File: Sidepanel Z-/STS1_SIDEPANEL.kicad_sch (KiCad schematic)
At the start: 5 parts, among them J1 Conn_02x04_Odd_Even, J2 Conn_02x02_Odd_Even

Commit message: Review Ready for V2.0
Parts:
- J1: value Conn_02x04_Odd_Even -> (none); footprint SamacSys:M808280842 -> (none)
- J2: value Conn_02x02_Odd_Even -> (none); footprint USER_Passiv:M80-8280442 -> (none)
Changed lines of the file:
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@@
     (in_bom yes) (on_board yes) (fields_autoplaced)
     (property "Reference" "J1" (id 0) (at 40.64 60.96 0))
-    (property "Value" "Conn_02x04_Odd_Even" (id 1) (at 40.64 63.5 0))
-    (property "Footprint" "SamacSys:M808280842" (id 2) (at 39.37 69.85 0)
+    (property "Value" "" (id 1) (at 40.64 63.5 0))
+    (property "Footprint" "" (id 2) (at 39.37 69.85 0)
       (effects (font (size 1.27 1.27)) hide)
     )
@@
     (in_bom yes) (on_board yes) (fields_autoplaced)
     (property "Reference" "J2" (id 0) (at 86.36 66.04 0))
-    (property "Value" "Conn_02x02_Odd_Even" (id 1) (at 86.36 68.58 0))
-    (property "Footprint" "USER_Passiv:M80-8280442" (id 2) (at 85.09 72.39 0)
+    (property "Value" "" (id 1) (at 86.36 68.58 0))
+    (property "Footprint" "" (id 2) (at 85.09 72.39 0)
       (effects (font (size 1.27 1.27)) hide)
     )
@@
     (path "/" (page "1"))
     (path "/9d03bb93-a9aa-424f-bd25-022f173efd1d" (page "3"))
+    (path "/4f87559b-6bba-4ff6-97a7-dad9a308db2d" (page "4"))
     (path "/13fd01c2-9c13-4b4c-bd8b-0bea989ca11e" (page "4"))
-    (path "/4f87559b-6bba-4ff6-97a7-dad9a308db2d" (page "4"))
   )
   (symbol_instances
@@
     )
     (path "/4f87559b-6bba-4ff6-97a7-dad9a308db2d/934b6342-5d8d-49da-bf4f-f7fa77f16f34"
-      (reference "CUR1") (unit 1) (value "TMCS1101A3BQDT") (footprint "SOIC127P600X175-8N")
+      (reference "CUR1") (unit 1) (value "TMCS1101A3BQDT") (footprint "Package_SO:SOIC-8_3.9x4.9mm_P1.27mm")
     )
     (path "/4f87559b-6bba-4ff6-97a7-dad9a308db2d/bf187b1f-09ac-46cb-aea3-5e2484509796"
-      (reference "CUR2") (unit 1) (value "TMCS1101A3BQDT") (footprint "SOIC127P600X175-8N")
+      (reference "CUR2") (unit 1) (value "TMCS1101A3BQDT") (footprint "Package_SO:SOIC-8_3.9x4.9mm_P1.27mm")
     )
     (path "/4f87559b-6bba-4ff6-97a7-dad9a308db2d/a554cf31-0806-4740-ba0b-f0d59599f4ca"
@@
     )
     (path "/4f87559b-6bba-4ff6-97a7-dad9a308db2d/c6a198d2-e0e4-4d6d-8a2a-bdeb249501be"
-      (reference "DOUT1") (unit 1) (value "SMM4F5.0") (footprint "SamacSys:STMITE")
+      (reference "DOUT1") (unit 1) (value "SMM4F5.0") (footprint "Diode_SMD:D_0603_1608Metric")
     )
     (path "/4f87559b-6bba-4ff6-97a7-dad9a308db2d/65c76957-ccfc-4d5b-b7d9-2ee7c354f524"
-      (reference "DOUT2") (unit 1) (value "SMM4F5.0") (footprint "SamacSys:STMITE")
+      (reference "DOUT2") (unit 1) (value "SMM4F5.0") (footprint "LED_SMD:LED_0603_1608Metric")
     )
     (path "/9d03bb93-a9aa-424f-bd25-022f173efd1d/d9839939-8918-48f3-b4b2-d753b1d9a645"
-      (reference "IC1") (unit 1) (value "TMP112AQDRLRQ1") (footprint "SamacSys:SOTFL50P160X60-6N")
+      (reference "IC1") (unit 1) (value "TMP112AQDRLRQ1") (footprint "Package_TO_SOT_SMD:SOT-563")
     )
     (path "/7d4ab197-adca-450c-9fc5-7a95ff72b885"
-      (reference "J1") (unit 1) (value "Conn_02x04_Odd_Even") (footprint "SamacSys:M808280842")
+      (reference "J1") (unit 1) (value "Conn_02x04_Odd_Even") (footprint "STS_Connector:M808280842")
     )
     (path "/9272ccd5-e950-4f99-baec-47da7f19129b"
-      (reference "J2") (unit 1) (value "Conn_02x02_Odd_Even") (footprint "USER_Passiv:M80-8280442")
+      (reference "J2") (unit 1) (value "Conn_02x02_Odd_Even") (footprint "STS_Connector:M808280442")
     )
     (path "/4f87559b-6bba-4ff6-97a7-dad9a308db2d/bfe4e68f-4cef-4b31-adff-8df094bc3870"
-      (reference "L_IN1") (unit 1) (value "10u") (footprint "SamacSys:INDPM5650X530N")
+      (reference "L_IN1") (unit 1) (value "10u") (footprint "Inductor_SMD:L_0805_2012Metric")
     )
     (path "/4f87559b-6bba-4ff6-97a7-dad9a308db2d/06a966cd-4913-436b-a217-7ac14ca6801e"
-      (reference "L_IN2") (unit 1) (value "10u") (footprint "SamacSys:INDPM5650X530N")
+      (reference "L_IN2") (unit 1) (value "10u") (footprint "Inductor_SMD:L_0805_2012Metric")
     )
     (path "/4f87559b-6bba-4ff6-97a7-dad9a308db2d/679b2e27-da22-4f13-a86e-25be83598a10"
-      (reference "MPPT1") (unit 1) (value "SPV1040TTR") (footprint "SamacSys:SOP65P640X120-8N")
+      (reference "MPPT1") (unit 1) (value "SPV1040TTR") (footprint "Package_SO:TSSOP-8_4.4x3mm_P0.65mm")
     )
     (path "/4f87559b-6bba-4ff6-97a7-dad9a308db2d/f7af2bb9-8bee-4408-8a96-0d5862b66a63"
-      (reference "MPPT2") (unit 1) (value "SPV1040TTR") (footprint "SamacSys:SOP65P640X120-8N")
+      (reference "MPPT2") (unit 1) (value "SPV1040TTR") (footprint "Package_SO:TSSOP-8_4.4x3mm_P0.65mm")
     )
     (path "/6503b427-07c6-4391-8fa6-4757fb4daa6c"
@@
     )
     (path "/4f87559b-6bba-4ff6-97a7-dad9a308db2d/e7b54c2f-482e-4a97-841f-62a80e0193a8"
-      (reference "SC1") (unit 1) (value "Solar_Cell") (footprint "USER_Activ:3G30A_40x80")
+      (reference "SC1") (unit 1) (value "Solar_Cell") (footprint "STS_Connector:3G30A_40x80")
     )
     (path "/4f87559b-6bba-4ff6-97a7-dad9a308db2d/3ad17c33-30d5-4097-824f-a9c26e6ca325"
-      (reference "SC2") (unit 1) (value "Solar_Cell") (footprint "USER_Activ:3G30A_40x80")
+      (reference "SC2") (unit 1) (value "Solar_Cell") (footprint "STS_Connector:3G30A_40x80")
     )
     (path "/e6cad5c9-4a9d-4066-8345-4481317e7bc0"
@@
     )
     (path "/9d03bb93-a9aa-424f-bd25-022f173efd1d/a83d6342-0e16-4131-8bb9-e65e4d72dab0"
-      (reference "U1") (unit 1) (value "GUVA-C32SM") (footprint "USER_Optic:OLGA 2mm x 2,3mm")
-    )
-  )
+      (reference "U1") (unit 1) (value "GUVA-C32SM") (footprint "Package_SO:SO-4_4.4x3.6mm_P2.54mm")
+    )
+  )

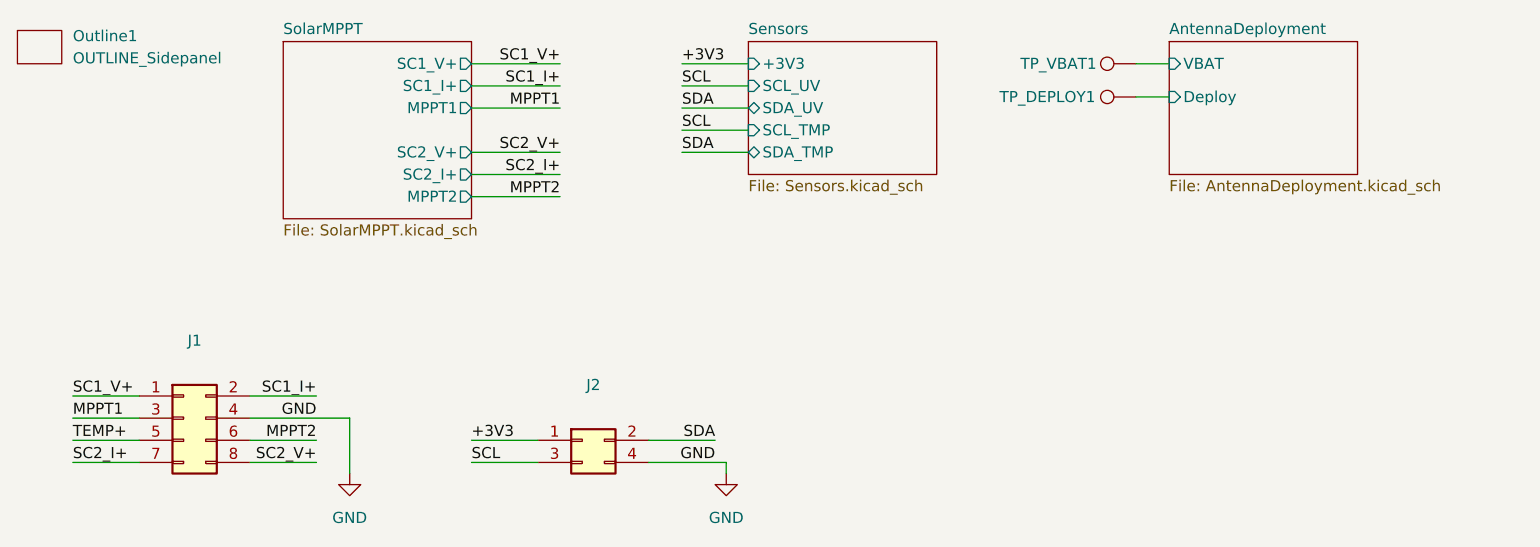
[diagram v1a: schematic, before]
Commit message: Paar Fehler behoben, Z+ no MOSFET
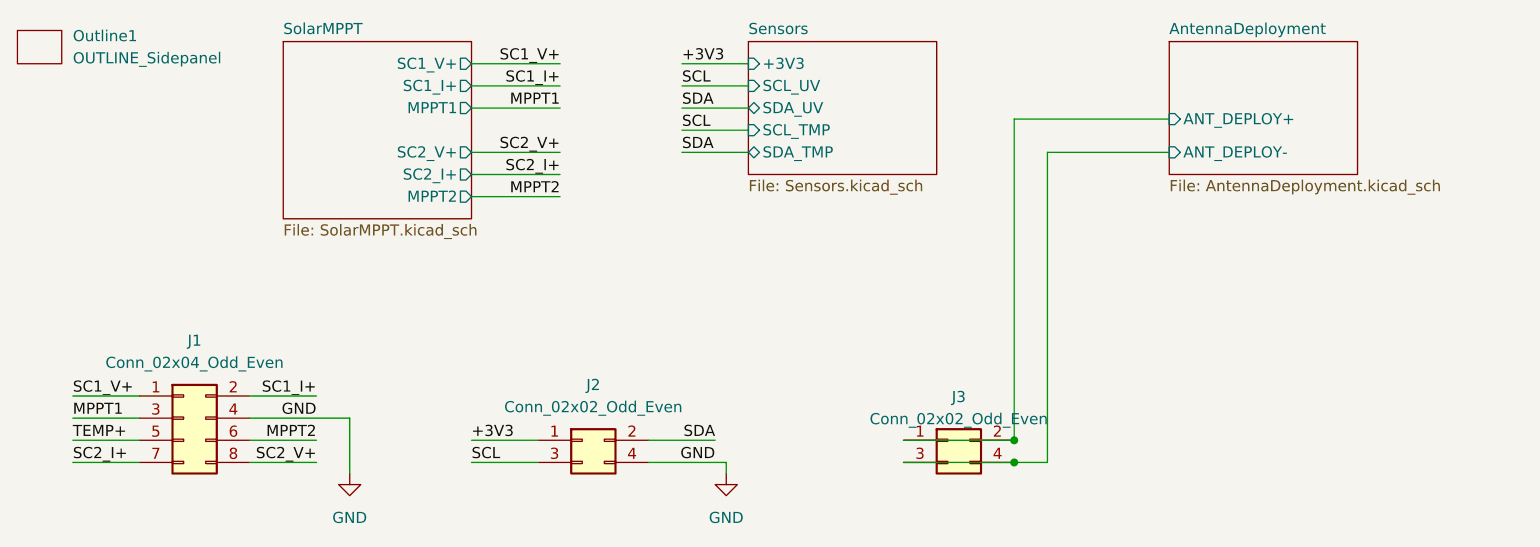
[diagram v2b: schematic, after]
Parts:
- removed TP_DEPLOY1, TP_VBAT1: TestPoint, TestPoint:TestPoint_Loop_D1.80mm_Drill1.0mm_Beaded, symbol Connector:TestPoint
- added J3: Conn_02x02_Odd_Even, STS_Connector:M808280442, symbol Connector_Generic:Conn_02x02_Odd_Even
- J1: value (none) -> Conn_02x04_Odd_Even; footprint (none) -> STS_Connector:M808280842
- J2: value (none) -> Conn_02x02_Odd_Even; footprint (none) -> STS_Connector:M808280442
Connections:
- new net AntennaDeployment/ANT_DEPLOY+: J3.1 (Pin_1), J3.2 (Pin_2)
- new net AntennaDeployment/ANT_DEPLOY-: J3.3 (Pin_3), J3.4 (Pin_4)
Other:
- sheet AntennaDeployment ports: added ANT_DEPLOY+, ANT_DEPLOY-; removed Deploy, VBAT
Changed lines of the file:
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@@
 (kicad_sch (version 20211123) (generator eeschema)
   (paper "A4")
+  (junction (at 134.62 74.93) (diameter 0) (color 0 0 0 0)
+  )
+  (junction (at 134.62 72.39) (diameter 0) (color 0 0 0 0)
+  )
+  (wire (pts (xy 121.92 74.93) (xy 134.62 74.93))
+    (stroke (width 0) (type default) (color 0 0 0 0))
+  )
   (wire (pts (xy 26.67 67.31) (xy 34.29 67.31))
     (stroke (width 0) (type default) (color 0 0 0 0))
   )
+  (wire (pts (xy 138.43 39.37) (xy 152.4 39.37))
+    (stroke (width 0) (type default) (color 0 0 0 0))
+  )
   (wire (pts (xy 54.61 74.93) (xy 46.99 74.93))
     (stroke (width 0) (type default) (color 0 0 0 0))
@@
     (stroke (width 0) (type default) (color 0 0 0 0))
   )
+  (wire (pts (xy 134.62 35.56) (xy 152.4 35.56))
+    (stroke (width 0) (type default) (color 0 0 0 0))
+  )
   (wire (pts (xy 72.39 39.37) (xy 82.55 39.37))
     (stroke (width 0) (type default) (color 0 0 0 0))
@@
     (stroke (width 0) (type default) (color 0 0 0 0))
   )
+  (wire (pts (xy 138.43 74.93) (xy 138.43 39.37))
+    (stroke (width 0) (type default) (color 0 0 0 0))
+  )
+  (wire (pts (xy 134.62 74.93) (xy 138.43 74.93))
+    (stroke (width 0) (type default) (color 0 0 0 0))
+  )
   (wire (pts (xy 72.39 31.75) (xy 82.55 31.75))
     (stroke (width 0) (type default) (color 0 0 0 0))
@@
     (stroke (width 0) (type default) (color 0 0 0 0))
   )
+  (wire (pts (xy 134.62 72.39) (xy 134.62 35.56))
+    (stroke (width 0) (type default) (color 0 0 0 0))
+  )
   (wire (pts (xy 92.71 72.39) (xy 100.33 72.39))
     (stroke (width 0) (type default) (color 0 0 0 0))
   )
-  (wire (pts (xy 148.59 33.02) (xy 152.4 33.02))
-    (stroke (width 0) (type default) (color 0 0 0 0))
-  )
-  (wire (pts (xy 148.59 29.21) (xy 152.4 29.21))
+  (wire (pts (xy 121.92 72.39) (xy 134.62 72.39))
     (stroke (width 0) (type default) (color 0 0 0 0))
   )
@@
     (in_bom yes) (on_board yes) (fields_autoplaced)
     (property "Reference" "J1" (id 0) (at 40.64 60.96 0))
-    (property "Value" "" (id 1) (at 40.64 63.5 0))
-    (property "Footprint" "" (id 2) (at 39.37 69.85 0)
+    (property "Value" "Conn_02x04_Odd_Even" (id 1) (at 40.64 63.5 0))
+    (property "Footprint" "STS_Connector:M808280842" (id 2) (at 39.37 69.85 0)
       (effects (font (size 1.27 1.27)) hide)
     )
@@
     (in_bom yes) (on_board yes) (fields_autoplaced)
     (property "Reference" "J2" (id 0) (at 86.36 66.04 0))
-    (property "Value" "" (id 1) (at 86.36 68.58 0))
-    (property "Footprint" "" (id 2) (at 85.09 72.39 0)
+    (property "Value" "Conn_02x02_Odd_Even" (id 1) (at 86.36 68.58 0))
+    (property "Footprint" "STS_Connector:M808280442" (id 2) (at 85.09 72.39 0)
       (effects (font (size 1.27 1.27)) hide)
     )
@@
     (pin "4")
   )
+  (symbol (lib_id "Connector_Generic:Conn_02x02_Odd_Even") (at 127 72.39 0) (unit 1)
+    (in_bom yes) (on_board yes) (fields_autoplaced)
+    (property "Reference" "J3" (id 0) (at 128.27 67.4202 0))
+    (property "Value" "Conn_02x02_Odd_Even" (id 1) (at 128.27 69.9571 0))
+    (property "Footprint" "STS_Connector:M808280442" (id 2) (at 127 72.39 0)
+      (effects (font (size 1.27 1.27)) hide)
+    )
+    (property "Datasheet" "~" (id 3) (at 127 72.39 0)
+      (effects (font (size 1.27 1.27)) hide)
+    )
+    (pin "1")
+    (pin "2")
+    (pin "3")
+    (pin "4")
+  )
   (symbol (lib_id "power:GND") (at 101.6 76.2 0) (unit 1)
     (in_bom yes) (on_board yes) (fields_autoplaced)
@@
     )
     (property "Datasheet" "" (id 3) (at 101.6 76.2 0)
-      (effects (font (size 1.27 1.27)) hide)
-    )
-    (pin "1")
-  )
-  (symbol (lib_id "Connector:TestPoint") (at 148.59 29.21 90) (unit 1)
-    (in_bom yes) (on_board yes)
-    (property "Reference" "TP_VBAT1" (id 0) (at 139.7 29.21 90))
-    (property "Value" "TestPoint" (id 1) (at 145.288 25.4 90)
-      (effects (font (size 1.27 1.27)) hide)
-    )
-    (property "Footprint" "TestPoint:TestPoint_Loop_D1.80mm_Drill1.0mm_Beaded" (id 2) (at 148.59 24.13 0)
-      (effects (font (size 1.27 1.27)) hide)
-    )
-    (property "Datasheet" "~" (id 3) (at 148.59 24.13 0)
-      (effects (font (size 1.27 1.27)) hide)
-    )
-    (pin "1")
-  )
-  (symbol (lib_id "Connector:TestPoint") (at 148.59 33.02 90) (unit 1)
-    (in_bom yes) (on_board yes)
-    (property "Reference" "TP_DEPLOY1" (id 0) (at 138.43 33.02 90))
-    (property "Value" "TestPoint" (id 1) (at 145.288 29.21 90)
-      (effects (font (size 1.27 1.27)) hide)
-    )
-    (property "Footprint" "TestPoint:TestPoint_Loop_D1.80mm_Drill1.0mm_Beaded" (id 2) (at 148.59 27.94 0)
-      (effects (font (size 1.27 1.27)) hide)
-    )
-    (property "Datasheet" "~" (id 3) (at 148.59 27.94 0)
       (effects (font (size 1.27 1.27)) hide)
     )
@@
       (effects (font (size 1.27 1.27)) (justify left top))
     )
-    (pin "VBAT" input (at 152.4 29.21 180)
-      (effects (font (size 1.27 1.27)) (justify left))
-    )
-    (pin "Deploy" input (at 152.4 33.02 180)
+    (pin "ANT_DEPLOY+" input (at 152.4 35.56 180)
+      (effects (font (size 1.27 1.27)) (justify left))
+    )
+    (pin "ANT_DEPLOY-" input (at 152.4 39.37 180)
       (effects (font (size 1.27 1.27)) (justify left))
     )
@@
       (reference "#PWR04") (unit 1) (value "GND") (footprint "")
     )
-    (path "/13fd01c2-9c13-4b4c-bd8b-0bea989ca11e/8d918f42-aec3-43b4-b827-f06811b7b8dd"
-      (reference "#PWR05") (unit 1) (value "GND") (footprint "")
-    )
     (path "/4f87559b-6bba-4ff6-97a7-dad9a308db2d/f1d749a3-7f50-4988-a0b3-62f40a86408e"
       (reference "#PWR06") (unit 1) (value "GND") (footprint "")
@@
       (reference "J2") (unit 1) (value "Conn_02x02_Odd_Even") (footprint "STS_Connector:M808280442")
     )
+    (path "/bc26867e-2044-46bb-8920-dfb46ce37aad"
+      (reference "J3") (unit 1) (value "Conn_02x02_Odd_Even") (footprint "STS_Connector:M808280442")
+    )
     (path "/4f87559b-6bba-4ff6-97a7-dad9a308db2d/bfe4e68f-4cef-4b31-adff-8df094bc3870"
       (reference "L_IN1") (unit 1) (value "10u") (footprint "Inductor_SMD:L_0805_2012Metric")
@@
       (reference "Outline1") (unit 1) (value "OUTLINE_Sidepanel") (footprint "USER_OUTLINE:OUTLINE_SidepanelZ+")
     )
-    (path "/13fd01c2-9c13-4b4c-bd8b-0bea989ca11e/479e0940-045a-4a1c-b6d6-7097eb56969a"
-      (reference "Q1") (unit 1) (value "BSS214NW") (footprint "Package_TO_SOT_SMD:SOT-323_SC-70")
-    )
     (path "/4f87559b-6bba-4ff6-97a7-dad9a308db2d/548d9577-1c12-4167-8fdd-bb768e95bfba"
       (reference "R11") (unit 1) (value "1M") (footprint "Resistor_SMD:R_0603_1608Metric")
@@
       (reference "R32") (unit 1) (value "1k") (footprint "Resistor_SMD:R_0603_1608Metric")
     )
-    (path "/13fd01c2-9c13-4b4c-bd8b-0bea989ca11e/3f0f93d4-3a5b-4d68-b0c6-873c01f0f933"
-      (reference "RB1") (unit 1) (value "10k") (footprint "Resistor_SMD:R_0603_1608Metric")
-    )
     (path "/13fd01c2-9c13-4b4c-bd8b-0bea989ca11e/8b937a4c-4702-470b-b385-859583bbe895"
       (reference "RD1") (unit 1) (value "22R") (footprint "Resistor_SMD:R_MiniMELF_MMA-0204")
@@
       (reference "SC2") (unit 1) (value "Solar_Cell") (footprint "STS_Connector:3G30A_40x80")
     )
-    (path "/e6cad5c9-4a9d-4066-8345-4481317e7bc0"
-      (reference "TP_DEPLOY1") (unit 1) (value "TestPoint") (footprint "TestPoint:TestPoint_Loop_D1.80mm_Drill1.0mm_Beaded")
-    )
-    (path "/df05315c-0e06-4f7c-b891-155333895af1"
-      (reference "TP_VBAT1") (unit 1) (value "TestPoint") (footprint "TestPoint:TestPoint_Loop_D1.80mm_Drill1.0mm_Beaded")
-    )
     (path "/9d03bb93-a9aa-424f-bd25-022f173efd1d/a83d6342-0e16-4131-8bb9-e65e4d72dab0"
